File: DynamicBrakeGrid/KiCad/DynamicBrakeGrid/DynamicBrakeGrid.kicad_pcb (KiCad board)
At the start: 2 copper layers, 240 x 120 mm, 124 parts, among them IC3 UCC27424QDRQ1, IC5 LM358DR, IC6 MCP2515-e_ST, IC7 TJA1050T_CM,118, IC8 LM358DR, J1 1987724, J10 5442251, J11 5442251, J12 5442251, J13 38969-0002, J16 1548129, J17 1548129, J2 1987724, J22 1548129, J23 1548129, J24 5442251, J25 5442251, J3 1987724, J4 1987724, J5 5442251, J6 5442251, J7 5442251, J8 5442251, J9 5442251, M1 Fan_4pin, M2 Fan_4pin, M3 Fan_4pin, M8 Fan_4pin, Q1 STWA75N60M6, Q2 STWA75N60M6, U6 ACS758xCB-200U-PFF, Y1 8MHz

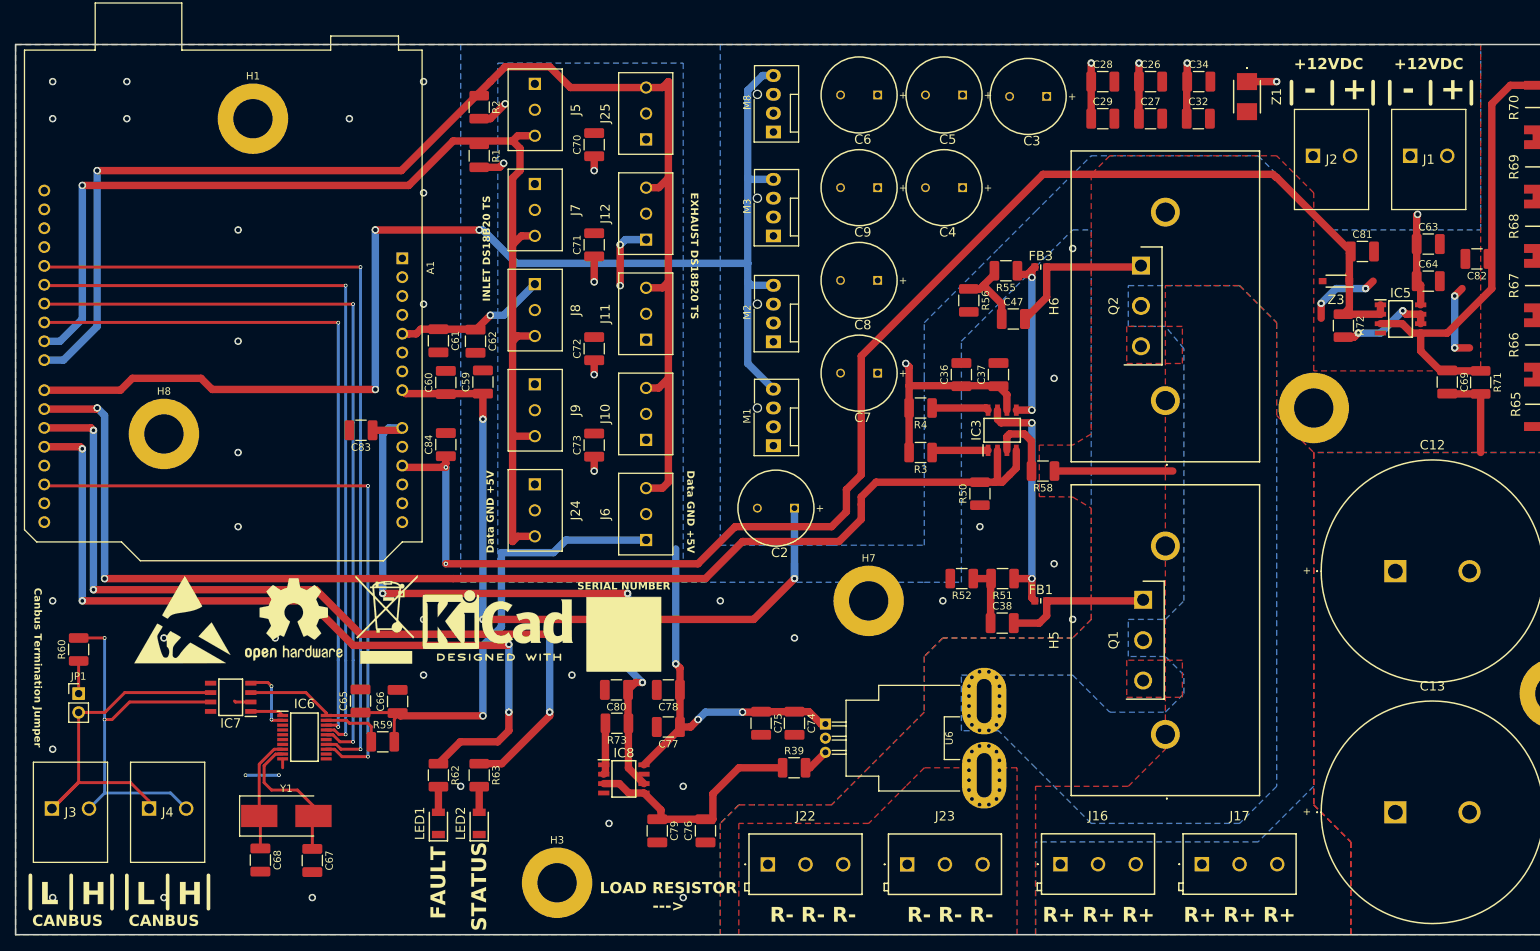
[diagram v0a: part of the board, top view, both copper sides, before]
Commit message: Update Schematics, Inverter, Gate Driver, Mechanical, Software
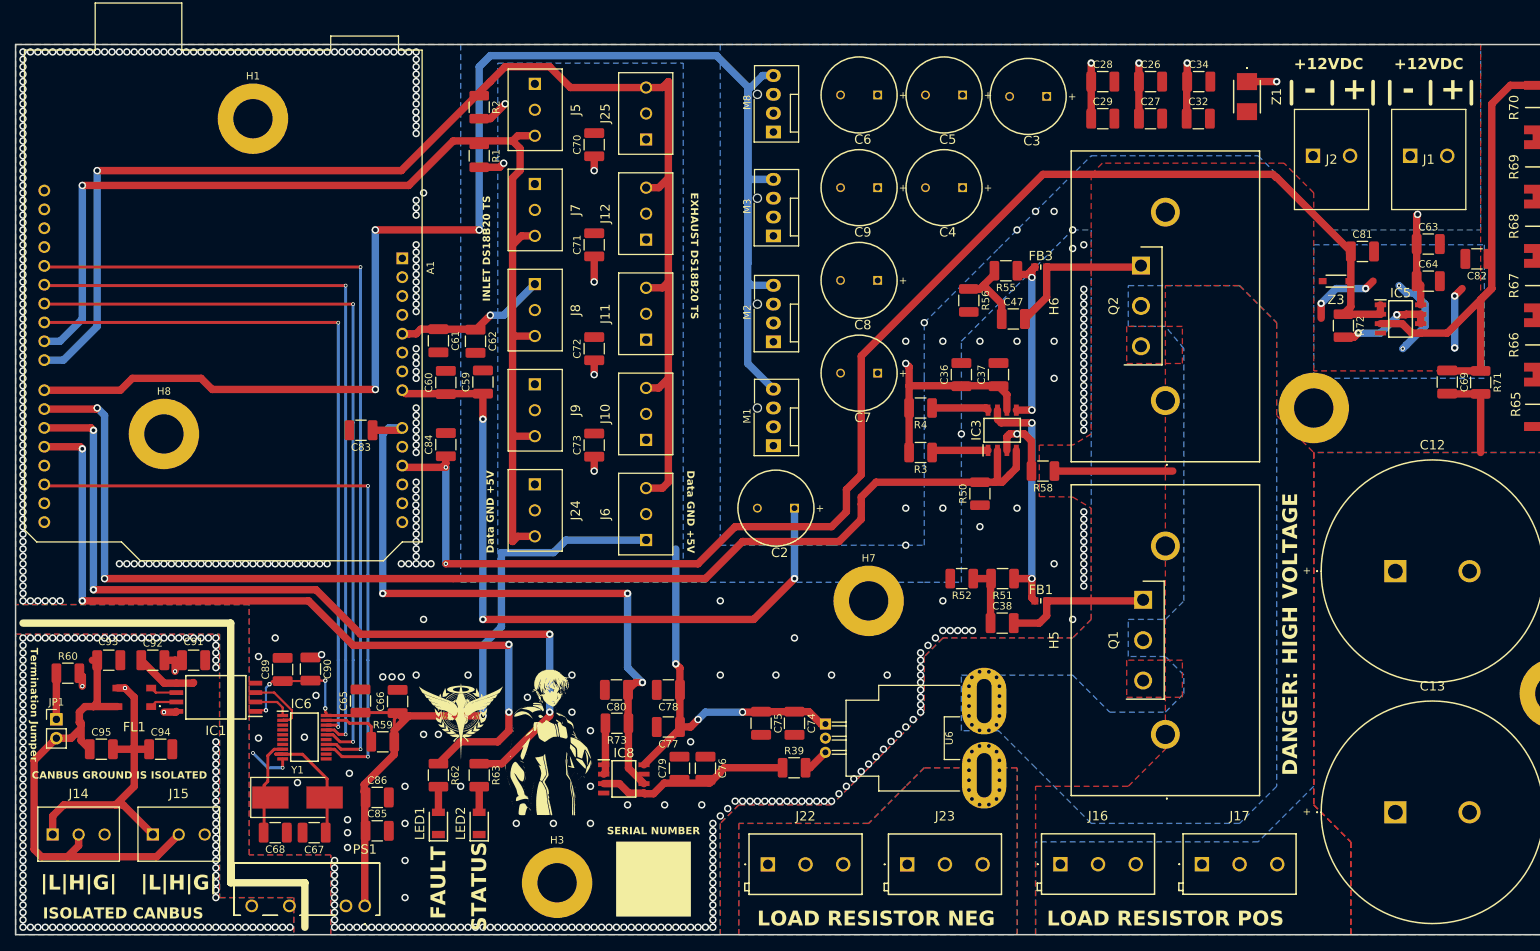
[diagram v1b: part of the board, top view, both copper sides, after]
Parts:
- removed IC7: TJA1050T_CM,118, InverterCom:SOIC127P600X175-8N
- removed J3, J4: 1987724, InverterCom:1987724
- added C85: 100nF, Capacitor_SMD:C_1210_3225Metric_Pad1.33x2.70mm_HandSolder, F.Cu at (78.8, 146.0)
- added C86: 10uF, Capacitor_SMD:C_1210_3225Metric_Pad1.33x2.70mm_HandSolder, F.Cu at (78.8, 141.5)
- added C89: 100nF, Capacitor_SMD:C_1210_3225Metric_Pad1.33x2.70mm_HandSolder, F.Cu at (66.0, 124.2)
- added C90: 10uF, Capacitor_SMD:C_1210_3225Metric_Pad1.33x2.70mm_HandSolder, F.Cu at (69.8, 124.2)
- added C91: 10uF, Capacitor_SMD:C_1210_3225Metric_Pad1.33x2.70mm_HandSolder, F.Cu at (54.0, 123.0)
- added C92: 100nF, Capacitor_SMD:C_1210_3225Metric_Pad1.33x2.70mm_HandSolder, F.Cu at (48.5, 123.0)
- added C93: 22pF, Capacitor_SMD:C_1210_3225Metric_Pad1.33x2.70mm_HandSolder, F.Cu at (42.6, 123.0)
- added C94: 22pF, Capacitor_SMD:C_1210_3225Metric_Pad1.33x2.70mm_HandSolder, F.Cu at (49.6, 135.0)
- added C95: 22pF, Capacitor_SMD:C_1210_3225Metric_Pad1.33x2.70mm_HandSolder, F.Cu at (41.6, 135.0)
- added FL1: ACT45B-101-2P-TL003, InverterCom:ACT45B1012PTL003, F.Cu at (46.0, 128.0)
- added G***: LOGO, InverterCom:ra, F.Cu at (102.0, 133.0)
- added G***: LOGO, InverterCom:Silkscreen_Logo_CelstialBeing_S, F.Cu at (90.0, 131.0)
- added G***: LOGO, InverterCom:Silkscreen_Logo_CelstialBeing_S, B.Cu at (234.0, 88.0)
- added IC1: ISO1042BDWVR, InverterCom:SOIC127P1150X280-8N, F.Cu at (57.0, 128.0)
- added J14: 5442251, InverterCom:5442251, F.Cu at (35.0, 146.5)
- added J15: 5442251, InverterCom:5442251, F.Cu at (48.5, 146.5)
- added PS1: RFMM-0505S, InverterCom:RFMM0505S, F.Cu at (77.1, 156.1)
- REF** (x4): moved to B.Cu
- moved REF** 208.2 mm to (248.0, 46.0), turned to 180 degrees
- moved REF** 207.8 mm to (263.0, 47.0), turned to 180 degrees
- moved REF** 153.2 mm to (230.0, 45.0), turned to 180 degrees
- moved REF** 151.9 mm to (214.0, 46.0), turned to 180 degrees
- moved C79 8.95 mm to (119.5, 137.6), turned to 90 degrees
- moved C76 8.44 mm to (123.0, 137.6), turned to -90 degrees
- moved JP1 4.59 mm to (35.5, 131.0)
- moved C68 4.19 mm to (65.0, 146.2), turned to 0 degrees
- moved C67 3.76 mm to (70.2, 146.2), turned to 180 degrees
- moved R60 3.51 mm to (37.0, 124.8), turned to 0 degrees
- moved Y1 2.92 mm to (68.0, 141.5)
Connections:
- JP1 pad 2: CanL_External -> CanH_External
- R60 pad 2: CanH_External -> CanL_External
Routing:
- net FAN_PWM: track 172.7 -> 219.0 mm
- net +5V: track 180.5 -> 206.1 mm, vias 13 -> 15
- net CanH_External: track 54.5 -> 62.9 mm, vias 2 -> 0
- net CANBUS_ISO_GND: track 0.00 -> 8.38 mm, vias 0 -> 128
- net GND: track 38.4 -> 46.2 mm, vias 40 -> 437
- net CANBUS_ISO_5V: track 0.00 -> 5.59 mm, vias 0 -> 2
- net Net-(IC8-IN1+): track 31.7 -> 26.2 mm
- net Net-(IC5-IN1+): track 61.6 -> 67.1 mm
- net Net-(IC6-OSC1): track 19.2 -> 15.7 mm
- net Net-(IC1-CANH): track 0.00 -> 2.90 mm
- net Net-(IC1-CANL): track 0.00 -> 2.90 mm
- net Net-(IC6-OSC2): track 15.4 -> 13.0 mm
- net +12V: track 162.7 -> 160.7 mm
- net Net-(JP1-A): track 4.40 -> 6.22 mm
- net CanL_External: track 50.0 -> 48.8 mm, vias 0 -> 2
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- added copper zone on B.Cu, net CANBUS_ISO_5V
- added copper zone on F.Cu, net CANBUS_ISO_GND
- added copper zone on In1.Cu, net CANBUS_ISO_GND
- added copper zone on In2.Cu, net CANBUS_ISO_GND
- added copper zone on In1.Cu, net DC_LINK_V+
- added copper zone on In1.Cu, net GND
- added copper zone on In2.Cu, net GND
- added copper zone on In2.Cu, net GNDPWR
- added copper zone on In1.Cu, net Net-(Q1-D)
- added copper zone on B.Cu, net RESISTOR_RETURN
- added copper zone on In1.Cu, net RESISTOR_RETURN
- added copper zone on In2.Cu, net RESISTOR_RETURN
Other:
- copper layers 2 -> 4
- board text added: "CANBUS GROUND IS ISOLATED"
- board text added: "DANGER: HIGH VOLTAGE"
- board text added: "ISOLATED CANBUS"
- board text added: "LOAD RESISTOR NEG"
- board text added: "LOAD RESISTOR POS"
- board text added: "Termination Jumper"
- board text added: "|L|H|G|"
- board text removed: "CANBUS"
- board text removed: "Canbus Termination Jumper"
- board text removed: "H"
- board text removed: "L"
- board text removed: "LOAD RESISTOR --->"
- board text removed: "R+ R+ R+"
- board text removed: "R- R- R-"
